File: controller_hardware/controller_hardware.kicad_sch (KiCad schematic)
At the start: 8 parts, among them J1 USB_C_Receptacle_USB2.0_16P, J2 110-87-318-41-001101, J3 0532610471, J4 532610671, U1 ESP32-S3-MINI-1-N8, U2 D3V3XA4B10LP, U3 TLV75801PDRV

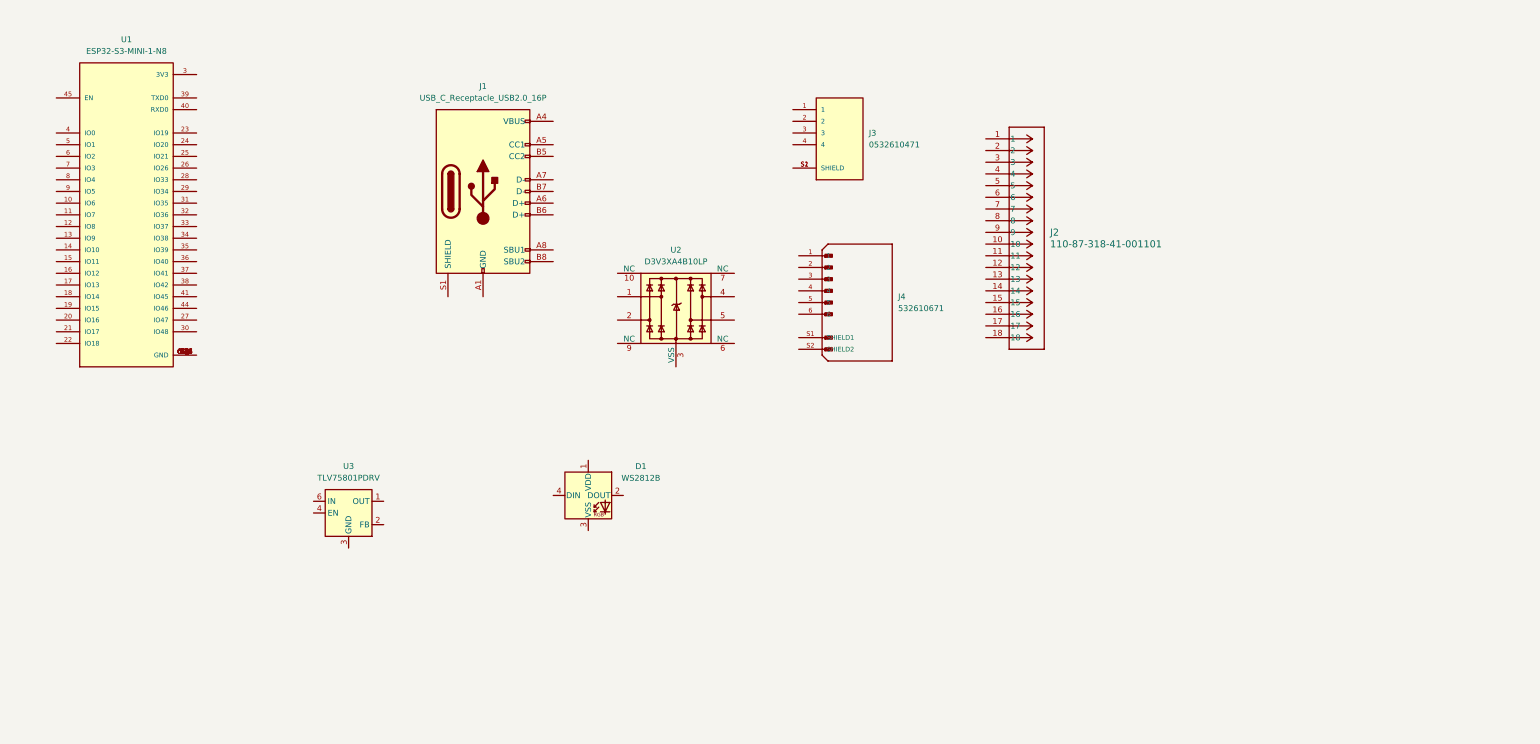
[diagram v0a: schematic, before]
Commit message: added more eda and spice models
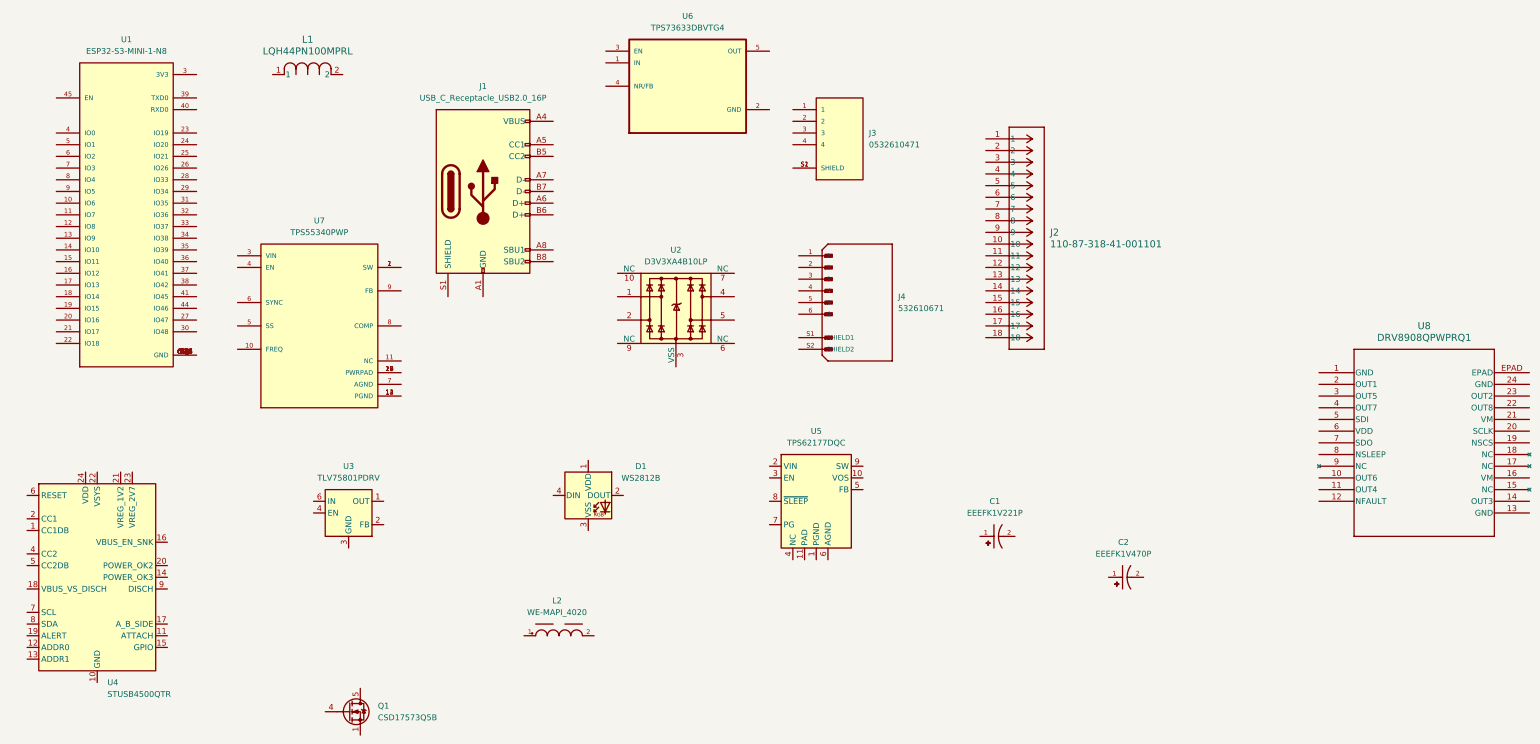
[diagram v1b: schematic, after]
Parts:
- added C1: EEEFK1V221P, EEEFK1V221P:CAP_EEEFK1V221P, symbol EEEFK1V221P:EEEFK1V221P
- added C2: EEEFK1V470P, EEEFK1V470P:CAP_EEEFK1V470P, symbol EEEFK1V470P:EEEFK1V470P
- added L1: LQH44PN100MPRL, IND_LQH44PN_PR_MUR, symbol 2025-04-27_19-46-57:LQH44PN100MPRL
- added L2: WE-MAPI_4020, WE-MAPI_4020:WE-MAPI_4020, symbol 74438357047:WE-MAPI_4020
- added Q1: CSD17573Q5B, Package_TO_SOT_SMD:TDSON-8-1, symbol Transistor_FET:CSD17573Q5B
- added U4: STUSB4500QTR, Package_DFN_QFN:QFN-24-1EP_4x4mm_P0.5mm_EP2.7x2.7mm, symbol Interface_USB:STUSB4500QTR
- added U5: TPS62177DQC, Package_SON:WSON-10-1EP_2x3mm_P0.5mm_EP0.84x2.4mm_ThermalVias, symbol Regulator_Switching:TPS62177DQC
- added U6: TPS73633DBVTG4, TPS73633DBVTG4:SOT95P280X145-5N, symbol TPS73633DBVTG4:TPS73633DBVTG4
- added U7: TPS55340PWP, TPS55340PWP:IC_TPS55340PWP, symbol TPS55340PWP:TPS55340PWP
- added U8: DRV8908QPWPRQ1, PWP24_4P5X7P9_TEX, symbol DRV8908BQPW:DRV8908QPWPRQ1
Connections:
- new net: U4.10 (GND), U4.25 (GND)
- new net: U7.1 (SW), U7.2 (SW)
- new net: U7.12 (PGND), U7.13 (PGND), U7.14 (PGND)
- new net: U7.15 (PWRPAD), U7.16 (PWRPAD), U7.17 (PWRPAD), U7.18 (PWRPAD), U7.19 (PWRPAD), U7.20 (PWRPAD), U7.21 (PWRPAD)
- new net: Q1.1 (S), Q1.2 (S), Q1.3 (S)

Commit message: just pushing for fun
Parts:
- removed C1: EEEFK1V221P, EEEFK1V221P:CAP_EEEFK1V221P, symbol EEEFK1V221P:EEEFK1V221P
- removed C2: EEEFK1V470P, EEEFK1V470P:CAP_EEEFK1V470P, symbol EEEFK1V470P:EEEFK1V470P
- removed D1: WS2812B, LED_SMD:LED_WS2812B_PLCC4_5.0x5.0mm_P3.2mm, symbol LED:WS2812B
- removed J1: USB_C_Receptacle_USB2.0_16P, Connector_USB:USB_C_Receptacle_GCT_USB4105-xx-A_16P_TopMnt_Horizontal, symbol Connector:USB_C_Receptacle_USB2.0_16P
- removed J2: 110-87-318-41-001101, CONN18_318-41-001101_PRD, symbol 2025-04-26_22-41-39:110-87-318-41-001101
- removed J3: 0532610471, 0532610471:MOLEX_0532610471, symbol 0532610471:0532610471
- removed J4: 532610671, 532610671:MOLEX_532610671, symbol 0532610671:532610671
- removed L1: LQH44PN100MPRL, IND_LQH44PN_PR_MUR, symbol 2025-04-27_19-46-57:LQH44PN100MPRL
- removed L2: WE-MAPI_4020, WE-MAPI_4020:WE-MAPI_4020, symbol 74438357047:WE-MAPI_4020
- removed Q1: CSD17573Q5B, Package_TO_SOT_SMD:TDSON-8-1, symbol Transistor_FET:CSD17573Q5B
- removed U1: ESP32-S3-MINI-1-N8, ESP32-S3-MINI-1-N8:XCVR_ESP32-S3-MINI-1-N8, symbol ESP32-S3-MINI-1-N8:ESP32-S3-MINI-1-N8
- removed U2: D3V3XA4B10LP, Package_DFN_QFN:Diodes_UDFN-10_1.0x2.5mm_P0.5mm, symbol Power_Protection:D3V3XA4B10LP
- removed U3: TLV75801PDRV, Package_SON:WSON-6-1EP_2x2mm_P0.65mm_EP1x1.6mm, symbol Regulator_Linear:TLV75801PDRV
- removed U4: STUSB4500QTR, Package_DFN_QFN:QFN-24-1EP_4x4mm_P0.5mm_EP2.7x2.7mm, symbol Interface_USB:STUSB4500QTR
- removed U5: TPS62177DQC, Package_SON:WSON-10-1EP_2x3mm_P0.5mm_EP0.84x2.4mm_ThermalVias, symbol Regulator_Switching:TPS62177DQC
- removed U6: TPS73633DBVTG4, TPS73633DBVTG4:SOT95P280X145-5N, symbol TPS73633DBVTG4:TPS73633DBVTG4
- removed U7: TPS55340PWP, TPS55340PWP:IC_TPS55340PWP, symbol TPS55340PWP:TPS55340PWP
- removed U8: DRV8908QPWPRQ1, PWP24_4P5X7P9_TEX, symbol DRV8908BQPW:DRV8908QPWPRQ1
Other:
- added sheet USB-C (USB-C.kicad_sch)
